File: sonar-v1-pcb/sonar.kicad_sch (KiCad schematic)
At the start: 14 parts, among them J101 DF40C-80DS-0.4V51, U1 XT60_M

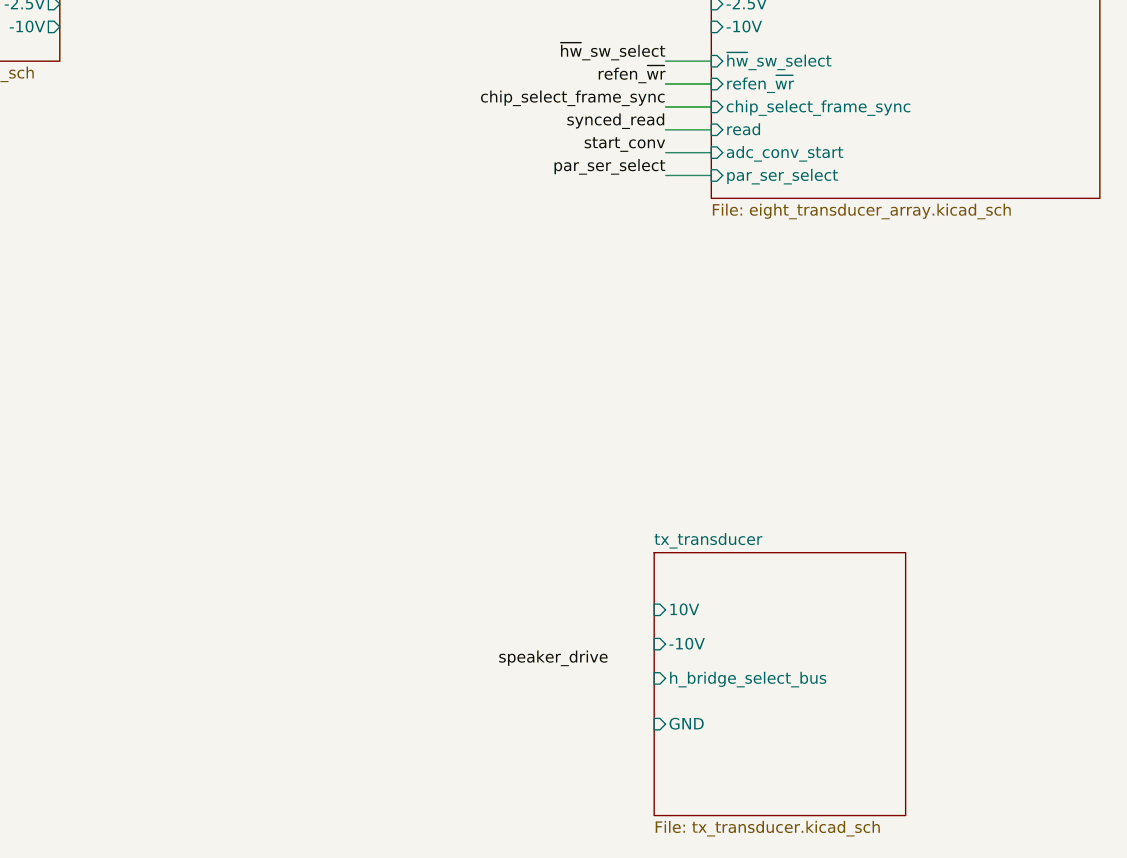
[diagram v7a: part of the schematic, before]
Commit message: Add an h-bridge
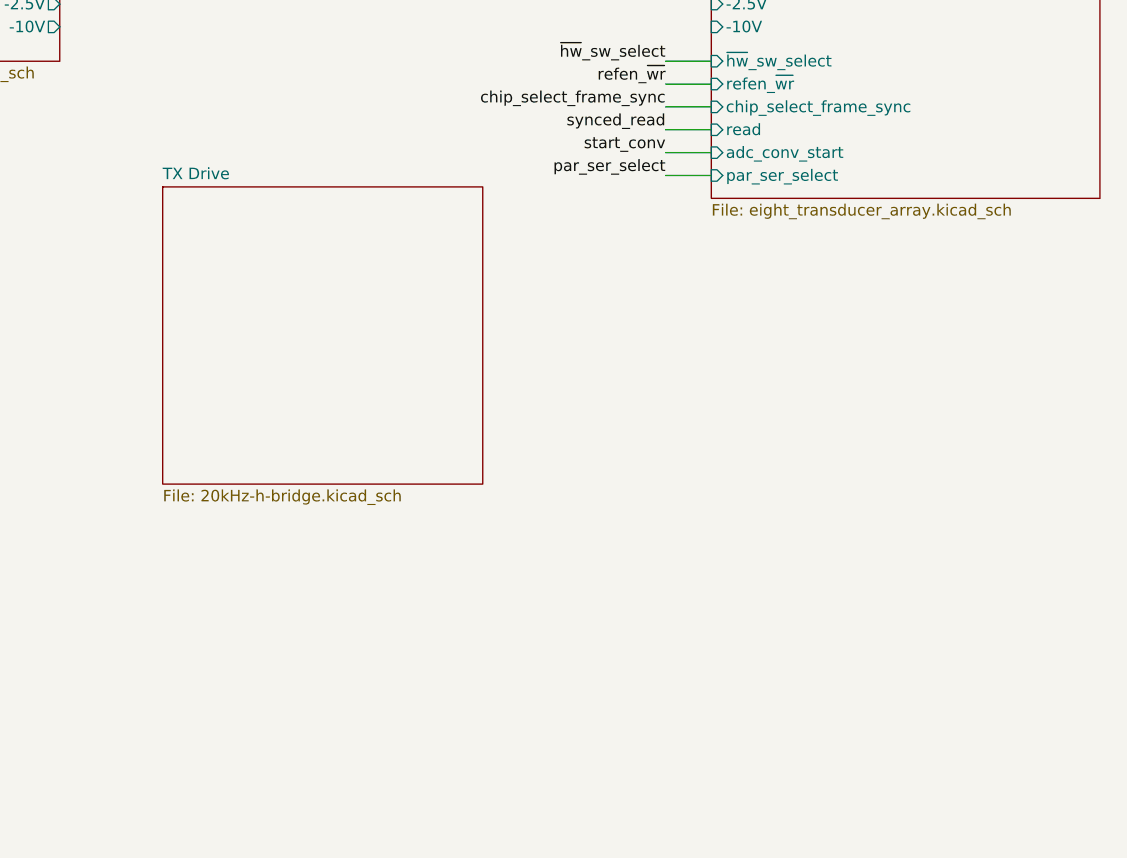
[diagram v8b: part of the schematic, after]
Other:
- removed sheet tx_transducer
- added sheet TX Drive (20kHz-h-bridge.kicad_sch)
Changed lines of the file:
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@@
 		)
 	)
-	(label "speaker_drive"
-		(at 231.14 218.44 180)
-		(effects
-			(font
-				(size 1.27 1.27)
-			)
-			(justify right bottom)
-		)
-	)
 	(label "chip_select_frame_sync"
 		(at 237.49 156.21 180)
@@
 	)
 	(sheet
-		(at 236.22 205.74)
-		(size 27.94 29.21)
+		(at 181.61 165.1)
+		(size 35.56 33.02)
 		(exclude_from_sim no)
 		(in_bom yes)
@@
 		)
 		(fill
-			(color 0 0 0 0)
+			(color 157 224 255 1)
 		)
-		(property "Sheetname" "tx_transducer"
-			(at 236.22 205.0284 0)
+		(property "Sheetname" "TX Drive"
+			(at 181.61 164.3884 0)
 			(show_name no)
 			(do_not_autoplace no)
@@
 			)
 		)
-		(property "Sheetfile" "tx_transducer.kicad_sch"
-			(at 236.22 235.5346 0)
+		(property "Sheetfile" "20kHz-h-bridge.kicad_sch"
+			(at 181.61 198.7046 0)
 			(show_name no)
 			(do_not_autoplace no)
@@
 			)
 		)
-		(pin "10V" input
-			(at 236.22 212.09 180)
-			(effects
-				(font
-					(size 1.27 1.27)
-				)
-				(justify left)
-			)
-		)
-		(pin "-10V" input
-			(at 236.22 215.9 180)
-			(effects
-				(font
-					(size 1.27 1.27)
-				)
-				(justify left)
-			)
-		)
-		(pin "h_bridge_select_bus" input
-			(at 236.22 219.71 180)
-			(effects
-				(font
-					(size 1.27 1.27)
-				)
-				(justify left)
-			)
-		)
-		(pin "GND" input
-			(at 236.22 224.79 180)
-			(effects
-				(font
-					(size 1.27 1.27)
-				)
-				(justify left)
-			)
-		)
